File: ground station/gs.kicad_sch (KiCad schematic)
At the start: 35 parts, among them J1 USB_C_Receptacle_USB2.0_14P, J2 OLED, J4 H9161TR-ND, J7 Conn_02x03_Counter_Clockwise, U1 ATSAMD21G18A-A, U17 PE4259, U2 SX1262IMLTRT, U3 AMS1117-3.3, Y2 32MHz

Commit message: more pcb stuff's
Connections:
- net SCL: now also U1.32 (PA23)
- net SDA: now also U1.31 (PA22)
- no-connect marks 1 -> 24
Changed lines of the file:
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@@
+	)
+	(junction
+		(at 58.42 27.94)
+		(diameter 0)
+		(color 0 0 0 0)
 	)
 	(junction
@@
 	)
 	(no_connect
+		(at 33.02 40.64)
+	)
+	(no_connect
+		(at 68.58 58.42)
+	)
+	(no_connect
+		(at 68.58 43.18)
+	)
+	(no_connect
+		(at 68.58 40.64)
+	)
+	(no_connect
+		(at 33.02 63.5)
+	)
+	(no_connect
+		(at 33.02 86.36)
+	)
+	(no_connect
+		(at 33.02 48.26)
+	)
+	(no_connect
+		(at 33.02 58.42)
+	)
+	(no_connect
+		(at 33.02 45.72)
+	)
+	(no_connect
+		(at 33.02 38.1)
+	)
+	(no_connect
+		(at 33.02 73.66)
+	)
+	(no_connect
+		(at 68.58 91.44)
+	)
+	(no_connect
+		(at 33.02 35.56)
+	)
+	(no_connect
+		(at 68.58 93.98)
+	)
+	(no_connect
+		(at 68.58 60.96)
+	)
+	(no_connect
+		(at 33.02 55.88)
+	)
+	(no_connect
+		(at 68.58 55.88)
+	)
+	(no_connect
+		(at 33.02 43.18)
+	)
+	(no_connect
+		(at 33.02 60.96)
+	)
+	(no_connect
+		(at 68.58 63.5)
+	)
+	(no_connect
+		(at 33.02 106.68)
+	)
+	(no_connect
+		(at 33.02 50.8)
+	)
+	(no_connect
+		(at 33.02 104.14)
+	)
+	(no_connect
 		(at 132.08 55.88)
 	)
@@
 	(wire
 		(pts
-			(xy 53.34 27.94) (xy 55.88 27.94)
+			(xy 53.34 27.94) (xy 58.42 27.94)
 		)
 		(stroke
@@
 	(global_label "SCL"
 		(shape input)
-		(at 19.05 81.28 180)
-		(fields_autoplaced yes)
-		(effects
-			(font
-				(size 1.27 1.27)
-			)
-			(justify right)
-		)
-		(property "Intersheetrefs" "${INTERSHEET_REFS}"
-			(at 12.5572 81.28 0)
+		(at 33.02 93.98 180)
+		(fields_autoplaced yes)
+		(effects
+			(font
+				(size 1.27 1.27)
+			)
+			(justify right)
+		)
+		(property "Intersheetrefs" "${INTERSHEET_REFS}"
+			(at 26.5272 93.98 0)
 			(effects
 				(font
@@
 	(global_label "SDA"
 		(shape input)
-		(at 19.05 78.74 180)
-		(fields_autoplaced yes)
-		(effects
-			(font
-				(size 1.27 1.27)
-			)
-			(justify right)
-		)
-		(property "Intersheetrefs" "${INTERSHEET_REFS}"
-			(at 12.4967 78.74 0)
-			(effects
-				(font
+		(at 33.02 91.44 180)
+		(fields_autoplaced yes)
+		(effects
+			(font
+				(size 1.27 1.27)
+			)
+			(justify right)
+		)
+		(property "Intersheetrefs" "${INTERSHEET_REFS}"
+			(at 26.4667 91.44 0)
+			(effects
+				(font

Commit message: 60% of the routing is done
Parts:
- added BZ2: Buzzer, Buzzer_Beeper:MagneticBuzzer_PUI_AT-0927-TT-6-R, symbol Device:Buzzer
- added Q1: BSS138, Package_TO_SOT_SMD:SOT-23, symbol Transistor_FET:BSS138
- added R5: 2k2, Resistor_SMD:R_0603_1608Metric, symbol Device:R
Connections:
- net +3.3V: now also BZ2.1 (+)
- net BUZZER: now also Q1.1 (G), R5.1
- net GND: now also Q1.2 (S), R5.2
- new net: BZ2.2 (-), Q1.3 (D)
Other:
- note added: "Buzzer"

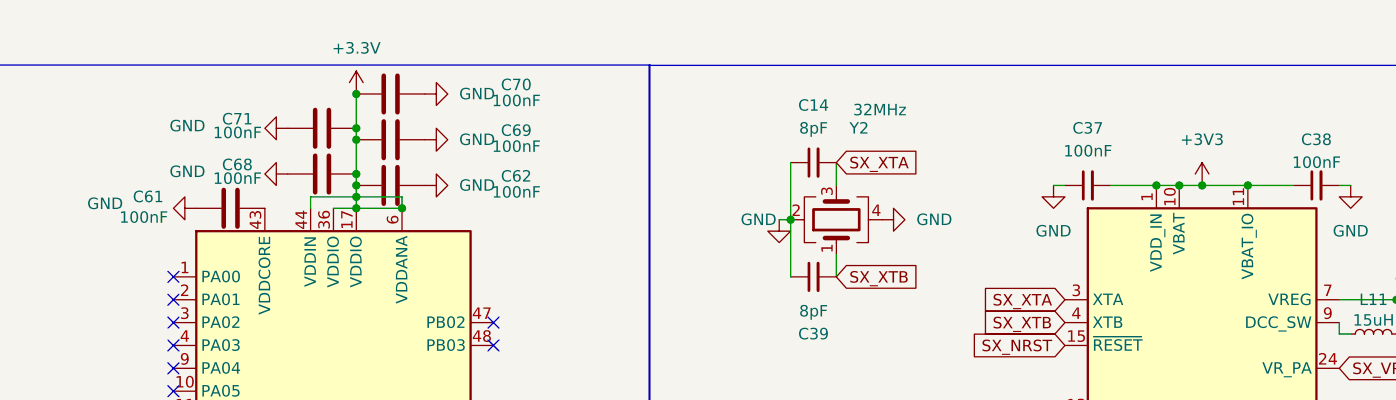
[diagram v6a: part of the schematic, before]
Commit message: I think the PCB is done for the ground station
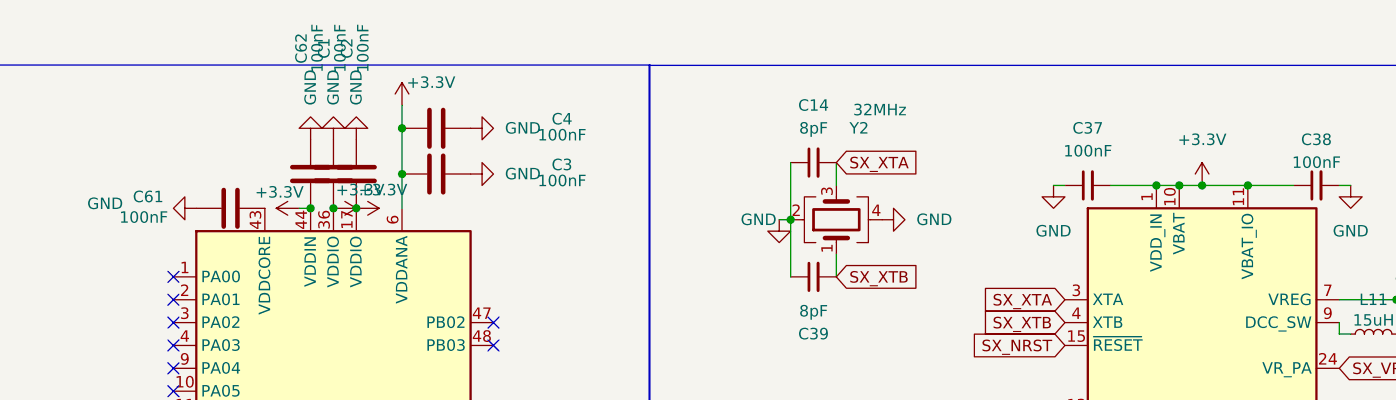
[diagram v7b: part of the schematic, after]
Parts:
- removed C68, C69, C70, C71: 100nF, Capacitor_SMD:C_0603_1608Metric, symbol Device:C
- added C1, C2, C3, C4: 100nF, Capacitor_SMD:C_0603_1608Metric, symbol Device:C
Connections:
- net +3V3 is gone; now on net +3.3V: C37.2, C38.1, U2.1 (VDD_IN), U2.10 (VBAT), U2.11 (VBAT_IO)
- net +3.3V: now also C1.2, C2.2, C3.2, C4.2
- net GND: now also C1.1, C2.1, C3.1, C4.1
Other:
- moved on the sheet: C62
